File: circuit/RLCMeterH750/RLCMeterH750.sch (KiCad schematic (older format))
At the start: 14 parts

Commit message: schematic continue
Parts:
- added C? (x4): 100n, Capacitor_SMD:C_0603_1608Metric, symbol Device:C
- added C?: 10u, Capacitor_SMD:C_1206_3216Metric, symbol Device:C
- added J?: ILI_9321(2.2inch), symbol Connector:Conn_01x09_Female
- added R? (x6): 33, Resistor_SMD:R_0603_1608Metric, symbol Device:R
- added SW?: PowerOn, balmer:SW_Angled_with_GND, symbol Switch:SW_SPDT
- added U?: LTC1550LCS8-2, Package_SO:SO-8_3.9x4.9mm_P1.27mm, symbol balmer:LTC1550LCS8
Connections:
- net labels added: -2V5, TFT_CS, TFT_D_C, TFT_MISO, TFT_MOSI, TFT_RESET, TFT_SCK
- wire segments 69 -> 115
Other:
- note added: "TFT_LED"
- note added: "Voltage inverter -2V\nMax 20 mA"
- moved on the sheet: BT?, C?, D?, R?, U?

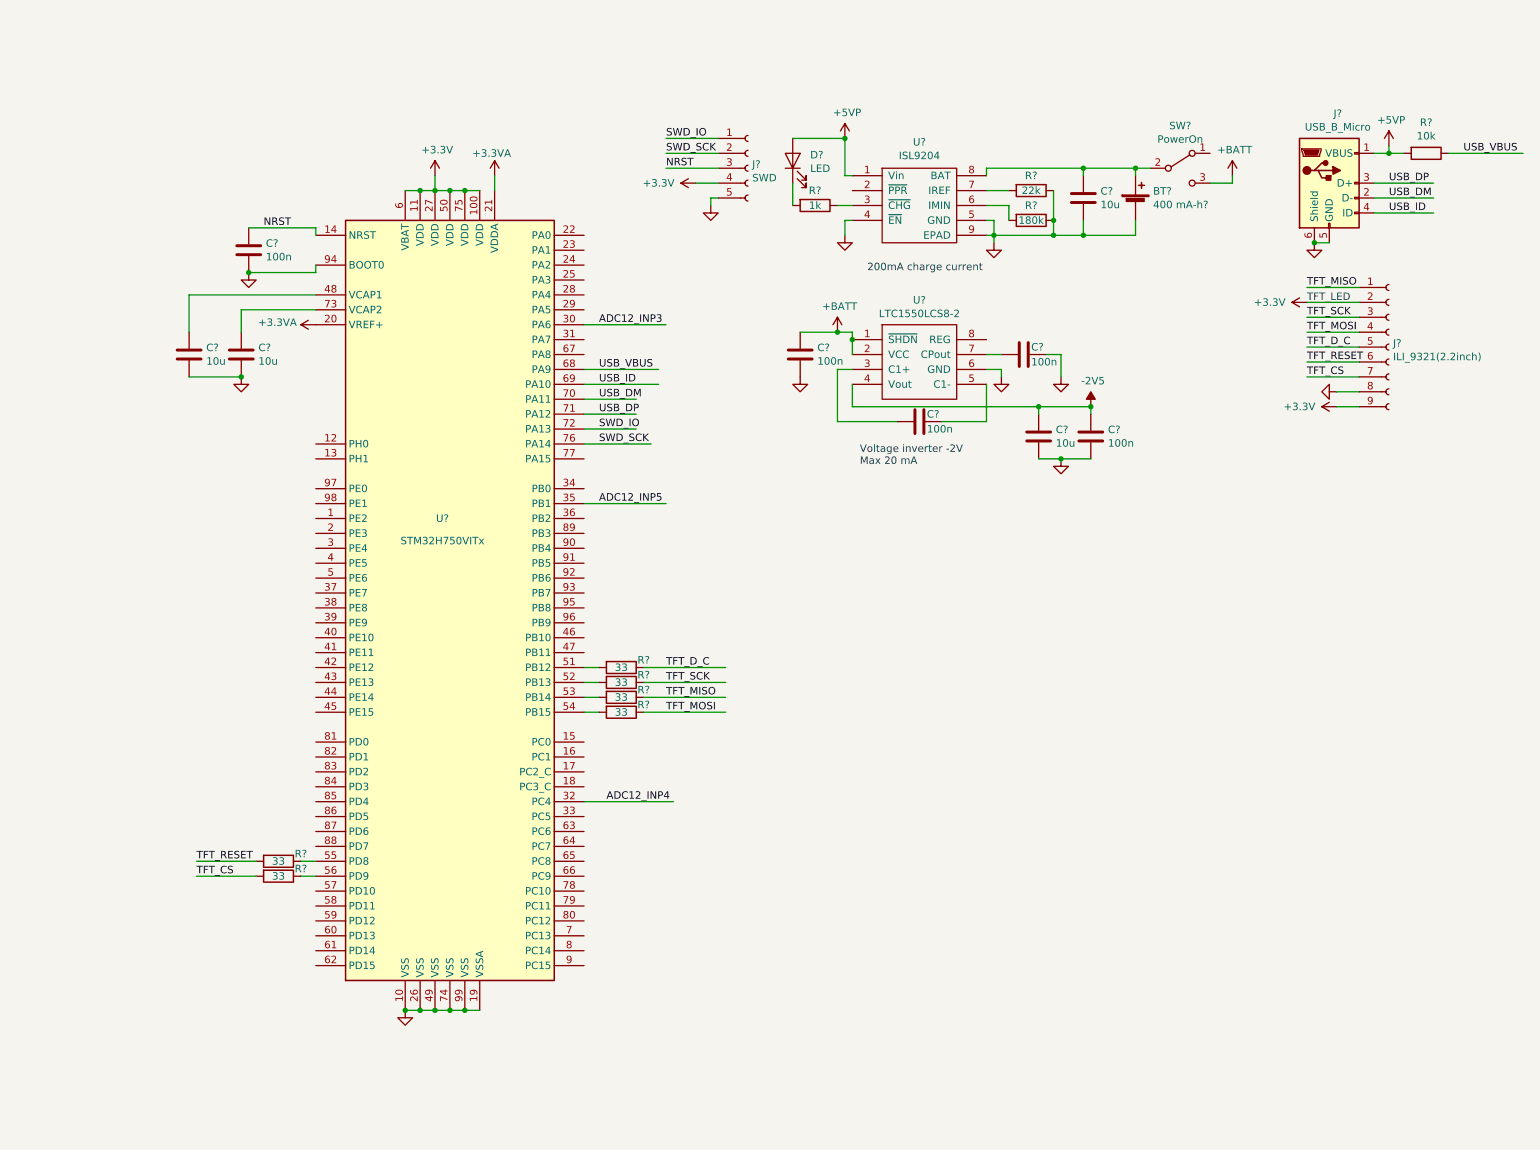
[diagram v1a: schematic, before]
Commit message: - crystal 25 MHz + AD9833
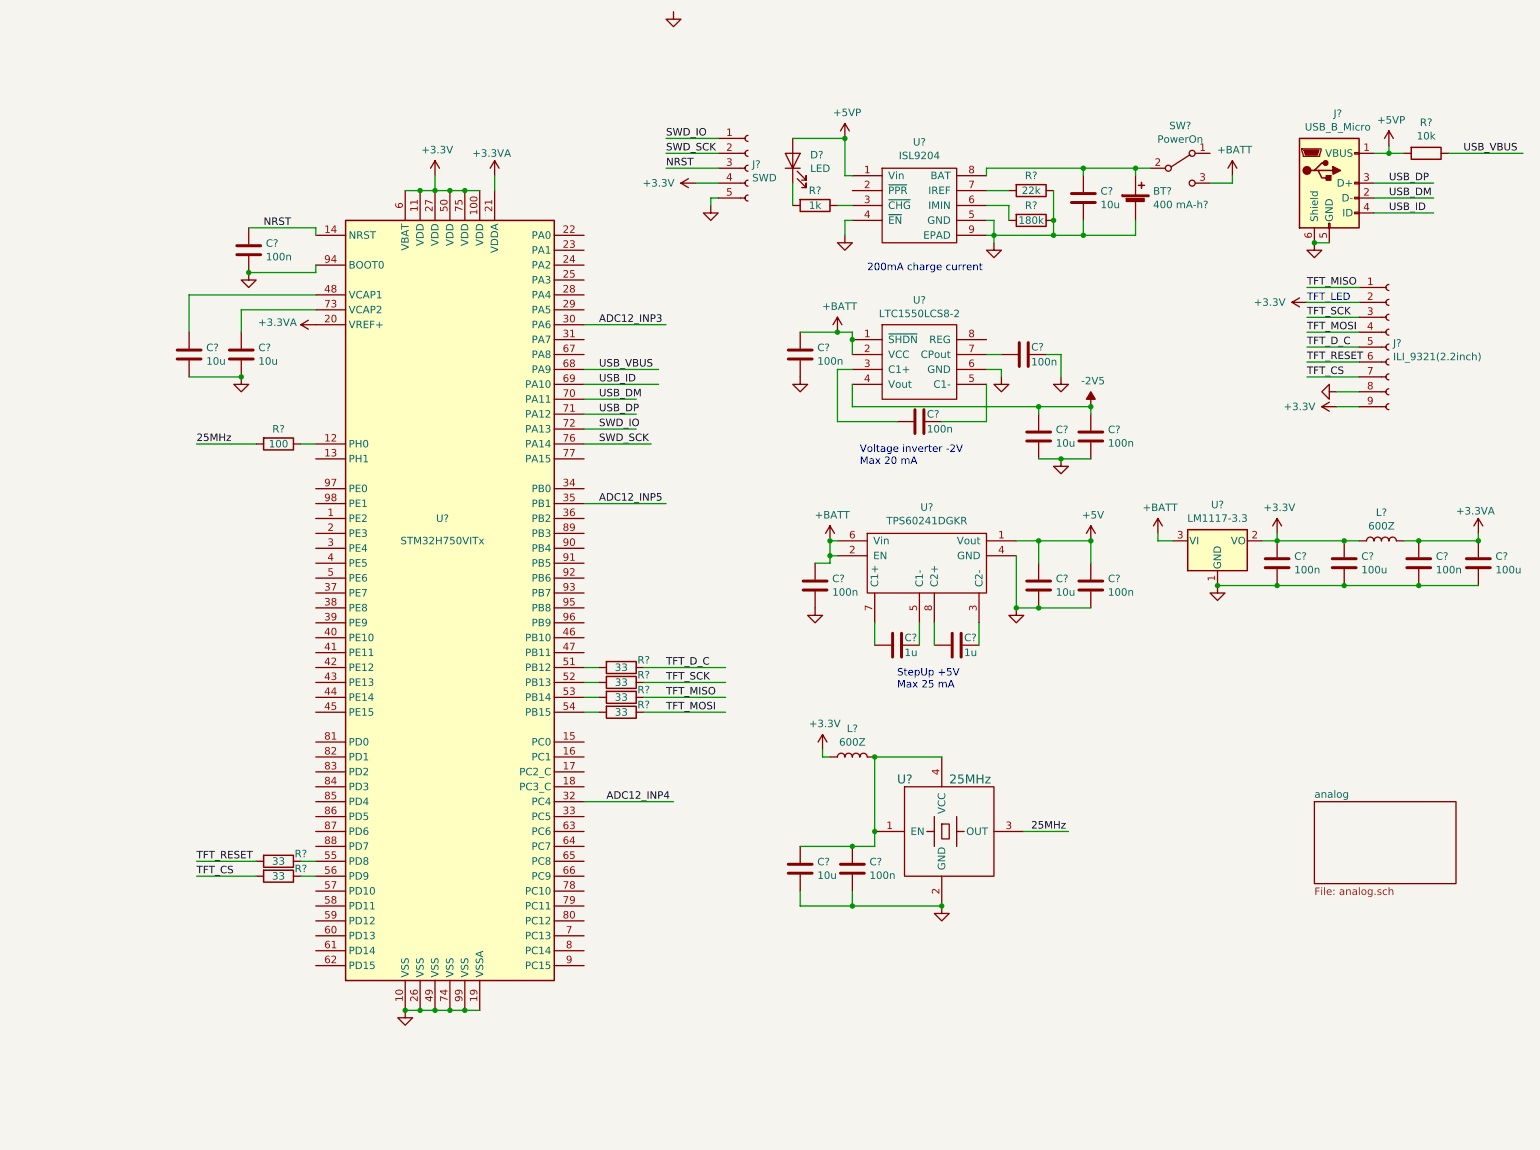
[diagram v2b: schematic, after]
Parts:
- added C? (x5): 100n, Capacitor_SMD:C_0603_1608Metric, symbol Device:C
- added C? (x2): 10u, Capacitor_SMD:C_1206_3216Metric, symbol Device:C
- added C? (x2): 100u, Capacitor_SMD:C_1206_3216Metric, symbol Device:C
- added C? (x2): 1u, Capacitor_SMD:C_0805_2012Metric, symbol Device:C
- added L? (x2): 600Z, Inductor_SMD:L_1206_3216Metric, symbol Device:L
- added R?: 100, Resistor_SMD:R_0603_1608Metric, symbol Device:R
- added U?: 25MHz, balmer:Crystal_5.0x3.2mm, symbol balmer:Crystal_Generator
- added U?: LM1117-3.3, Package_TO_SOT_SMD:SOT-223, symbol Regulator_Linear:LM1117-3.3
- added U?: TPS60241DGKR, Package_SO:TSSOP-8_3x3mm_P0.65mm, symbol balmer:TPS60241DGKR
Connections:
- net labels added: +5V, 25MHz
- wire segments 115 -> 158
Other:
- note added: "StepUp +5V\nMax 25 mA"

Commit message: - add encoder
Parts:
- added C? (x3): 22n, Capacitor_SMD:C_0603_1608Metric, symbol Device:C
- added R? (x3): 10k, Resistor_SMD:R_0603_1608Metric, symbol Device:R
- added SW?: EVQWKL001, balmer:Encoder_EVQWK4, symbol Device:Rotary_Encoder_Switch
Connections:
- net labels added: ENC_A, ENC_B, ENC_C
- wire segments 158 -> 179
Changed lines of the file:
@@
 Text Label 2050 2850 0    50   ~ 0
 25MHz
+$Comp
+L Device:Rotary_Encoder_Switch SW?
+U 1 1 5D9C2BDD
+P 5600 7050
+F 0 "SW?" H 5600 7417 50  0000 C CNN
+F 1 "EVQWKL001" H 5600 7326 50  0000 C CNN
+F 2 "balmer:Encoder_EVQWK4" H 5450 7210 50  0001 C CNN
+F 3 "~" H 5600 7310 50  0001 C CNN
+	1    5600 7050
+	1    0    0    -1
+$EndComp
+$Comp
+L Device:C C?
+U 1 1 5D9D807B
+P 4900 6900
+F 0 "C?" H 5015 6946 50  0000 L CNN
+F 1 "22n" H 5015 6855 50  0000 L CNN
+F 2 "Capacitor_SMD:C_0603_1608Metric" H 4938 6750 50  0001 C CNN
+F 3 "~" H 4900 6900 50  0001 C CNN
+	1    4900 6900
+	1    0    0    -1
+$EndComp
+$Comp
+L Device:C C?
+U 1 1 5D9DD258
+P 4900 7200
+F 0 "C?" H 5015 7246 50  0000 L CNN
+F 1 "22n" H 5015 7155 50  0000 L CNN
+F 2 "Capacitor_SMD:C_0603_1608Metric" H 4938 7050 50  0001 C CNN
+F 3 "~" H 4900 7200 50  0001 C CNN
+	1    4900 7200
+	1    0    0    -1
+$EndComp
+$Comp
+L Device:C C?
+U 1 1 5D9DD6BF
+P 6100 7050
+F 0 "C?" H 6215 7096 50  0000 L CNN
+F 1 "22n" H 6215 7005 50  0000 L CNN
+F 2 "Capacitor_SMD:C_0603_1608Metric" H 6138 6900 50  0001 C CNN
+F 3 "~" H 6100 7050 50  0001 C CNN
+	1    6100 7050
+	1    0    0    -1
+$EndComp
+Wire Wire Line
+	5900 6950 5900 6900
+Wire Wire Line
+	5900 6900 6000 6900
+Wire Wire Line
+	5900 7150 5900 7200
+Wire Wire Line
+	5900 7200 6100 7200
+Wire Wire Line
+	4900 7350 5300 7350
+Wire Wire Line
+	5300 7350 5300 7150
+Wire Wire Line
+	5300 7050 5200 7050
+Connection ~ 4900 7050
+Wire Wire Line
+	4900 6750 5300 6750
+Wire Wire Line
+	5300 6750 5300 6950
+$Comp
+L power:GND #PWR?
+U 1 1 5DA0647D
+P 6000 6900
+F 0 "#PWR?" H 6000 6650 50  0001 C CNN
+F 1 "GND" H 6005 6727 50  0001 C CNN
+F 2 "" H 6000 6900 50  0001 C CNN
+F 3 "" H 6000 6900 50  0001 C CNN
+	1    6000 6900
+	1    0    0    -1
+$EndComp
+Connection ~ 6000 6900
+Wire Wire Line
+	6000 6900 6100 6900
+$Comp
+L power:GND #PWR?
+U 1 1 5DA06A5A
+P 5200 7050
+F 0 "#PWR?" H 5200 6800 50  0001 C CNN
+F 1 "GND" H 5205 6877 50  0001 C CNN
+F 2 "" H 5200 7050 50  0001 C CNN
+F 3 "" H 5200 7050 50  0001 C CNN
+	1    5200 7050
+	1    0    0    -1
+$EndComp
+Connection ~ 5200 7050
+Wire Wire Line
+	5200 7050 4900 7050
+$Comp
+L Device:R R?
+U 1 1 5DA124D2
+P 4700 6750
+F 0 "R?" V 4600 6750 50  0000 C CNN
+F 1 "10k" V 4700 6750 50  0000 C CNN
+F 2 "Resistor_SMD:R_0603_1608Metric" V 4630 6750 50  0001 C CNN
+F 3 "~" H 4700 6750 50  0001 C CNN
+	1    4700 6750
+	0    1    1    0
+$EndComp
+$Comp
+L Device:R R?
+U 1 1 5DA15634
+P 4700 7350
+F 0 "R?" V 4600 7350 50  0000 C CNN
+F 1 "10k" V 4700 7350 50  0000 C CNN
+F 2 "Resistor_SMD:R_0603_1608Metric" V 4630 7350 50  0001 C CNN
+F 3 "~" H 4700 7350 50  0001 C CNN
+	1    4700 7350
+	0    1    1    0
+$EndComp
+Wire Wire Line
+	4550 7350 4550 7050
+Wire Wire Line
+	4900 6750 4850 6750
+Connection ~ 4900 6750
+Wire Wire Line
+	4900 7350 4850 7350
+Connection ~ 4900 7350
+$Comp
+L power:+3.3V #PWR?
+U 1 1 5DA37693
+P 4400 7050
+F 0 "#PWR?" H 4400 6900 50  0001 C CNN
+F 1 "+3.3V" H 4415 7223 50  0000 C CNN
+F 2 "" H 4400 7050 50  0001 C CNN
+F 3 "" H 4400 7050 50  0001 C CNN
+	1    4400 7050
+	1    0    0    -1
+$EndComp
+Wire Wire Line
+	4550 7050 4400 7050
+Connection ~ 4550 7050
+Wire Wire Line
+	4550 7050 4550 6750
+$Comp
+L power:+3.3V #PWR?
+U 1 1 5DA445DC
+P 6800 7200
+F 0 "#PWR?" H 6800 7050 50  0001 C CNN
+F 1 "+3.3V" H 6815 7373 50  0000 C CNN
+F 2 "" H 6800 7200 50  0001 C CNN
+F 3 "" H 6800 7200 50  0001 C CNN
+	1    6800 7200
+	1    0    0    -1
+$EndComp
+Text Label 5000 6750 0    50   ~ 0
+ENC_A
+Text Label 5000 7350 0    50   ~ 0
+ENC_B
+$Comp
+L Device:R R?
+U 1 1 5DA649A2
+P 6600 7200
+F 0 "R?" V 6500 7200 50  0000 C CNN
+F 1 "10k" V 6600 7200 50  0000 C CNN
+F 2 "Resistor_SMD:R_0603_1608Metric" V 6530 7200 50  0001 C CNN
+F 3 "~" H 6600 7200 50  0001 C CNN
+	1    6600 7200
+	0    1    1    0
+$EndComp
+Wire Wire Line
+	6100 7200 6450 7200
+Connection ~ 6100 7200
+Text Label 6200 7200 0    50   ~ 0
+ENC_C
+Wire Wire Line
+	6800 7200 6750 7200
+Wire Wire Line
+	4650 1450 5000 1450
+Text Label 4750 1450 0    50   ~ 0
+ENC_A
+Wire Wire Line
+	4650 1550 5000 1550
+Wire Wire Line
+	4650 1650 5000 1650
+Text Label 4750 1550 0    50   ~ 0
+ENC_B
+Text Label 4750 1650 0    50   ~ 0
+ENC_C
 $EndSCHEMATC

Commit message: -  то, что успели нарисовать в свободное время
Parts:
- added C23, C53, C54, C55, C56, C57: 100n, Capacitor_SMD:C_0603_1608Metric, symbol Device:C
- added U7: M25P16, Package_SO:SOIC-8_5.23x5.23mm_P1.27mm, symbol balmer:M25P16
- BT1: renamed from BT?; footprint (none) -> Connector_PinSocket_2.54mm:PinSocket_1x02_P2.54mm_Vertical
- D1: renamed from D?; footprint (none) -> LED_SMD:LED_0805_2012Metric_Pad1.15x1.40mm_HandSolder
- J3: renamed from J?; footprint (none) -> balmer:ILI_9321(2.2inch)
- gave numbers to parts that had none: 49
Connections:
- net labels added: DDS_FSYNC, DDS_SCLK, DDS_SDATA, ENC_S, FLASH_CS, FLASH_MISO, FLASH_MOSI, FLASH_SCK, S1, S2
- net labels removed: ENC_C
- wire segments 179 -> 217
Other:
- note added: "PB3 - SPI1_SCK \nPB4 - SPI1_MISO\nPB5 - SPI1_MOSI"
- note added: "PB6 - TIM4_CH1\nPB7 - TIM4_CH2"
- note added: "PC10 - SPI3_SCK\nPC11 - SPI3_MISO\nPC12 - SPI3_MOSI"

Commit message: - запустили код на STM32H750
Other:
- note added: "U3 Ошибка!!\nНужен был корпус\nTSSOP-8_3x3mm_P0.65mm"
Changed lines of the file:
@@
 Wire Wire Line
 	4700 3900 5000 3900
+Text Notes 7450 2100 0    50   ~ 0
+U3 Ошибка!!\nНужен был корпус\nTSSOP-8_3x3mm_P0.65mm
 $EndSCHEMATC
